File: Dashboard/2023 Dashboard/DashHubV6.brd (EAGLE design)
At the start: 86.4 x 66 mm, 33 parts, among them J1 LEFT, J2 RIGHT, U1 ALLEGRO_MICROSYSTEMS_ACS722LL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, U2 XBEE_PRO_S3B

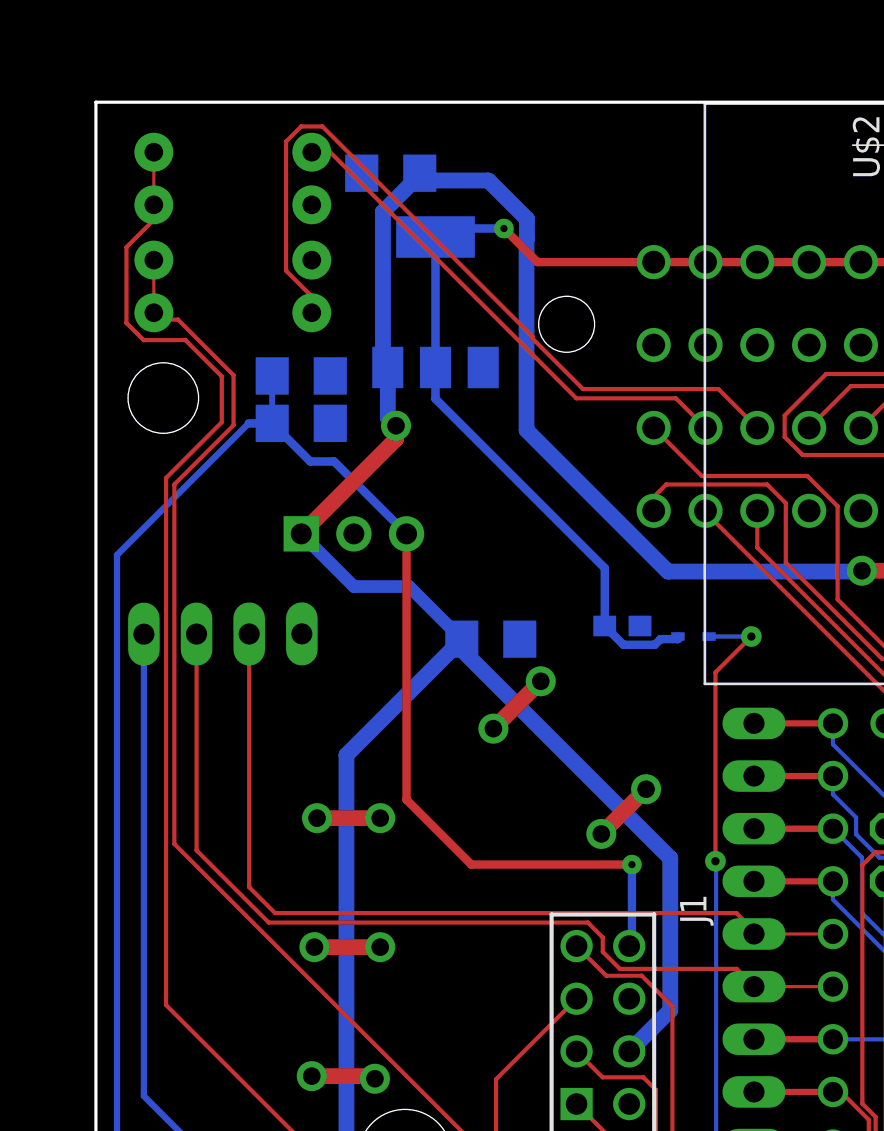
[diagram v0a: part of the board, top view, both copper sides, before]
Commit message: Updated pull ups on dashboard
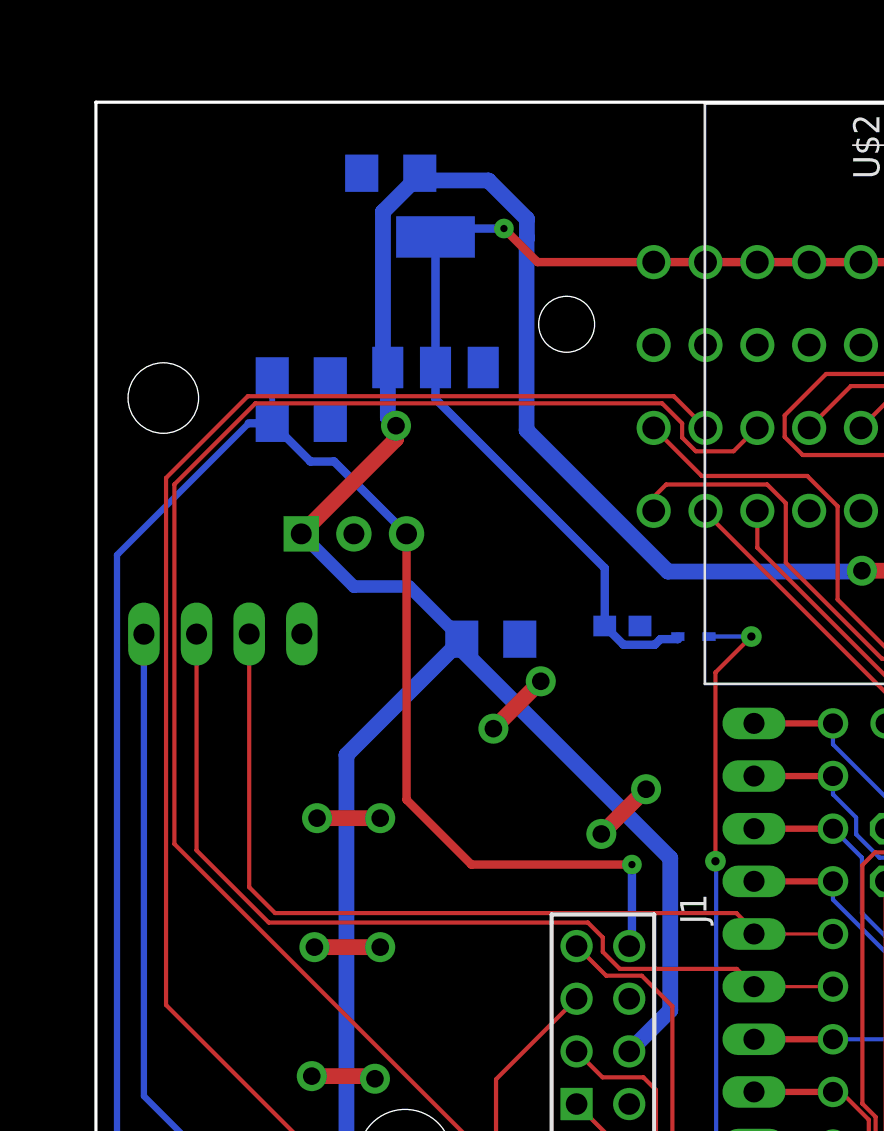
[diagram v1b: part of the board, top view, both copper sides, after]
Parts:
- removed R10, R11: 1.8k, SparkFun-Resistors:AXIAL-0.3
- removed R12, R13: 3.3k, SparkFun-Resistors:AXIAL-0.3
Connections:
- removed net N$23: R10.P$2, U$4.P$3B
- removed net N$24: R11.P$2, U$4.P$3C
- net ENGINE_RPM: now also U$4.P$3B; no longer R10.P$1, R12.P$2
- net GND: no longer R12.P$1, R13.P$1
- net SECONDARY_RPM: now also U$4.P$3C; no longer R11.P$1, R13.P$2
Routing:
- net N$24: track 37.9 -> 0.00 mm
- net N$23: track 24.5 -> 0.00 mm
- net SECONDARY_RPM: track 93.3 -> 110.8 mm
- net ENGINE_RPM: track 104.0 -> 111.8 mm
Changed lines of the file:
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@@
 <attribute name="VALUE" x="8.255" y="-31.242" size="1.27" layer="28" rot="MR90"/>
-</element>
-<element name="R10" library="SparkFun-Resistors" library_urn="urn:adsk.eagle:library:532" package="AXIAL-0.3" package3d_urn="urn:adsk.eagle:package:39658/1" value="1.8k" x="-36.576" y="30.607" smashed="yes" rot="MR180">
-<attribute name="NAME" x="-36.576" y="32.131" size="0.6096" layer="26" font="vector" ratio="20" rot="MR180" align="bottom-center"/>
-<attribute name="PROD_ID" value=" " x="-36.576" y="30.607" size="1.778" layer="28" rot="MR180" display="off"/>
-<attribute name="VALUE" x="-36.576" y="31.623" size="0.6096" layer="28" font="vector" ratio="20" rot="MR180" align="top-center"/>
-</element>
-<element name="R11" library="SparkFun-Resistors" library_urn="urn:adsk.eagle:library:532" package="AXIAL-0.3" package3d_urn="urn:adsk.eagle:package:39658/1" value="1.8k" x="-36.576" y="22.86" smashed="yes" rot="MR180">
-<attribute name="NAME" x="-36.576" y="24.384" size="0.6096" layer="26" font="vector" ratio="20" rot="MR180" align="bottom-center"/>
-<attribute name="PROD_ID" value=" " x="-36.576" y="22.86" size="1.778" layer="28" rot="MR180" display="off"/>
-<attribute name="VALUE" x="-36.576" y="23.876" size="0.6096" layer="28" font="vector" ratio="20" rot="MR180" align="top-center"/>
-</element>
-<element name="R12" library="SparkFun-Resistors" library_urn="urn:adsk.eagle:library:532" package="AXIAL-0.3" package3d_urn="urn:adsk.eagle:package:39658/1" value="3.3k" x="-36.576" y="28.067" smashed="yes" rot="MR0">
-<attribute name="NAME" x="-36.576" y="29.083" size="0.6096" layer="26" font="vector" ratio="20" rot="MR0" align="bottom-center"/>
-<attribute name="PROD_ID" value=" " x="-36.576" y="28.067" size="1.778" layer="28" rot="MR0" display="off"/>
-<attribute name="VALUE" x="-36.576" y="27.051" size="0.6096" layer="28" font="vector" ratio="20" rot="MR0" align="top-center"/>
-</element>
-<element name="R13" library="SparkFun-Resistors" library_urn="urn:adsk.eagle:library:532" package="AXIAL-0.3" package3d_urn="urn:adsk.eagle:package:39658/1" value="3.3k" x="-36.576" y="25.4" smashed="yes" rot="MR0">
-<attribute name="NAME" x="-36.576" y="26.416" size="0.6096" layer="26" font="vector" ratio="20" rot="MR0" align="bottom-center"/>
-<attribute name="PROD_ID" value=" " x="-36.576" y="25.4" size="1.778" layer="28" rot="MR0" display="off"/>
-<attribute name="VALUE" x="-36.576" y="24.384" size="0.6096" layer="28" font="vector" ratio="20" rot="MR0" align="top-center"/>
 </element>
 <element name="JP4" library="pinhead" library_urn="urn:adsk.eagle:library:325" package="2X05" package3d_urn="urn:adsk.eagle:package:22470/2" value="" x="0" y="-3.302" smashed="yes" rot="MR180">
@@
 <contactref element="J1" pad="02"/>
 <contactref element="JP2" pad="14"/>
-<contactref element="R12" pad="P$1"/>
-<contactref element="R13" pad="P$1"/>
 <contactref element="R14" pad="P$1"/>
 <contactref element="R16" pad="P$1"/>
@@
 </signal>
 <signal name="ENGINE_RPM">
-<contactref element="R10" pad="P$1"/>
-<contactref element="R12" pad="P$2"/>
 <contactref element="U$1" pad="22/A8"/>
 <contactref element="JP3" pad="5"/>
-<wire x1="-40.386" y1="30.607" x2="-40.386" y2="28.067" width="0.1524" layer="1"/>
 <wire x1="11.43" y1="-19.812" x2="7.62" y2="-19.812" width="0.3048" layer="1"/>
 <via x="-25.273" y="-21.59" extent="1-16" drill="0.35"/>
 <wire x1="-25.273" y1="-21.59" x2="-28.74636875" y2="-21.59" width="0.2032" layer="1"/>
 <wire x1="-28.74636875" y1="-21.59" x2="-39.796509375" y2="-10.539859375" width="0.2032" layer="1"/>
-<wire x1="-37.1094" y1="19.7860375" x2="-37.1094" y2="17.5773625" width="0.2032" layer="1"/>
-<wire x1="-40.88049375" y1="21.5392" x2="-41.7068" y2="22.36550625" width="0.2032" layer="1"/>
-<wire x1="-40.386" y1="27.34229375" x2="-40.386" y2="28.067" width="0.2032" layer="1"/>
-<wire x1="-41.7068" y1="26.02149375" x2="-40.386" y2="27.34229375" width="0.2032" layer="1"/>
-<wire x1="-37.1094" y1="19.7860375" x2="-38.8625625" y2="21.5392" width="0.2032" layer="1"/>
-<wire x1="-38.8625625" y1="21.5392" x2="-40.88049375" y2="21.5392" width="0.2032" layer="1"/>
-<wire x1="-41.7068" y1="22.36550625" x2="-41.7068" y2="26.02149375" width="0.2032" layer="1"/>
-<wire x1="-37.1094" y1="17.5773625" x2="-39.796509375" y2="14.890253125" width="0.2032" layer="1"/>
-<wire x1="-39.796509375" y1="14.890253125" x2="-39.796509375" y2="-10.539859375" width="0.2032" layer="1"/>
+<wire x1="-39.796509375" y1="-10.539859375" x2="-39.796509375" y2="14.890253125" width="0.2032" layer="1"/>
 <wire x1="-18.1864" y1="-23.4696" x2="3.9624" y2="-23.4696" width="0.2032" layer="16"/>
 <wire x1="3.9624" y1="-23.4696" x2="7.62" y2="-19.812" width="0.2032" layer="16"/>
@@
 <wire x1="-25.018165625" y1="-21.590834375" x2="-25.019" y2="-21.59" width="0.2032" layer="16"/>
 <wire x1="-25.273" y1="-21.59" x2="-25.019" y2="-21.59" width="0.2032" layer="16"/>
+<contactref element="U$4" pad="P$3B"/>
+<wire x1="-39.796509375" y1="14.890253125" x2="-35.85238125" y2="18.83438125" width="0.2032" layer="1"/>
+<wire x1="-35.85238125" y1="18.83438125" x2="-15.30038125" y2="18.83438125" width="0.2032" layer="1"/>
+<wire x1="-15.30038125" y1="18.83438125" x2="-13.77" y2="17.304" width="0.2032" layer="1"/>
 </signal>
 <signal name="AUX_TX">
@@
 </signal>
 <signal name="SECONDARY_RPM">
-<contactref element="R11" pad="P$1"/>
-<contactref element="R13" pad="P$2"/>
 <contactref element="U$1" pad="23/A9"/>
 <contactref element="JP3" pad="4"/>
-<wire x1="-40.386" y1="25.4" x2="-40.386" y2="22.86" width="0.1524" layer="1"/>
 <wire x1="11.43" y1="-22.352" x2="7.62" y2="-22.352" width="0.3048" layer="1"/>
 <via x="-19.177" y="-23.876" extent="1-16" drill="0.35"/>
-<wire x1="-39.2232625" y1="22.5298" x2="-40.0558" y2="22.5298" width="0.2032" layer="1"/>
-<wire x1="-40.0558" y1="22.5298" x2="-40.386" y2="22.86" width="0.2032" layer="1"/>
-<wire x1="-39.2232625" y1="22.5298" x2="-36.54073125" y2="19.84726875" width="0.2032" layer="1"/>
-<wire x1="-36.54073125" y1="19.84726875" x2="-36.54073125" y2="17.43426875" width="0.2032" layer="1"/>
 <wire x1="-39.3942" y1="14.5808" x2="-39.3942" y2="-2.7698" width="0.2032" layer="1"/>
-<wire x1="-36.54073125" y1="17.43426875" x2="-39.3942" y2="14.5808" width="0.2032" layer="1"/>
+<wire x1="-35.4844" y1="18.4906" x2="-39.3942" y2="14.5808" width="0.2032" layer="1"/>
 <wire x1="-39.3942" y1="-2.7698" x2="-24.257" y2="-17.907" width="0.2032" layer="1"/>
 <wire x1="-24.257" y1="-17.907" x2="-24.257" y2="-20.701" width="0.2032" layer="1"/>
@@
 <wire x1="-19.177" y1="-23.876" x2="-19.177" y2="-23.803" width="0.2032" layer="16"/>
 <wire x1="-19.177" y1="-23.803" x2="6.169" y2="-23.803" width="0.2032" layer="16"/>
+<contactref element="U$4" pad="P$3C"/>
+<wire x1="-14.8966" y1="16.83734375" x2="-14.23665625" y2="16.1774" width="0.2032" layer="1"/>
+<wire x1="-14.23665625" y1="16.1774" x2="-12.41434375" y2="16.1774" width="0.2032" layer="1"/>
+<wire x1="-11.28774375" y1="17.304" x2="-11.27" y2="17.304" width="0.2032" layer="1"/>
+<wire x1="-12.41434375" y1="16.1774" x2="-11.28774375" y2="17.304" width="0.2032" layer="1"/>
+<wire x1="-35.4844" y1="18.4906" x2="-15.86334375" y2="18.4906" width="0.2032" layer="1"/>
+<wire x1="-15.86334375" y1="18.4906" x2="-14.8966" y2="17.52385625" width="0.2032" layer="1"/>
+<wire x1="-14.8966" y1="17.52385625" x2="-14.8966" y2="16.83734375" width="0.2032" layer="1"/>
 </signal>
 <signal name="SIN_R">
@@
 <wire x1="11.43" y1="-27.432" x2="7.62" y2="-27.432" width="0.3048" layer="1"/>
 </signal>
-<signal name="N$23">
-<contactref element="R10" pad="P$2"/>
-<contactref element="U$4" pad="P$3B"/>
-<wire x1="-31.877" y1="30.607" x2="-32.766" y2="30.607" width="0.2032" layer="1"/>
-<wire x1="-31.877" y1="30.607" x2="-20.0025" y2="18.7325" width="0.2032" layer="1"/>
-<wire x1="-20.0025" y1="18.7325" x2="-15.1985" y2="18.7325" width="0.2032" layer="1"/>
-<wire x1="-15.1985" y1="18.7325" x2="-13.77" y2="17.304" width="0.2032" layer="1"/>
-</signal>
-<signal name="N$24">
-<contactref element="R11" pad="P$2"/>
-<contactref element="U$4" pad="P$3C"/>
-<wire x1="-34.0074" y1="31.12120625" x2="-33.28020625" y2="31.8484" width="0.2032" layer="1"/>
-<wire x1="-33.28020625" y1="31.8484" x2="-32.25179375" y2="31.8484" width="0.2032" layer="1"/>
-<wire x1="-32.766" y1="22.86" x2="-32.766" y2="23.64439375" width="0.2032" layer="1"/>
-<wire x1="-32.766" y1="23.64439375" x2="-34.0074" y2="24.88579375" width="0.2032" layer="1"/>
-<wire x1="-34.0074" y1="24.88579375" x2="-34.0074" y2="31.12120625" width="0.2032" layer="1"/>
-<wire x1="-22.1216" y1="21.71820625" x2="-22.1216" y2="21.61988125" width="0.2032" layer="1"/>
-<wire x1="-22.1216" y1="21.61988125" x2="-19.67871875" y2="19.177" width="0.2032" layer="1"/>
-<wire x1="-19.67871875" y1="19.177" x2="-13.143" y2="19.177" width="0.2032" layer="1"/>
-<wire x1="-32.25179375" y1="31.8484" x2="-22.1216" y2="21.71820625" width="0.2032" layer="1"/>
-<wire x1="-13.143" y1="19.177" x2="-11.27" y2="17.304" width="0.2032" layer="1"/>
-</signal>
 <signal name="33">

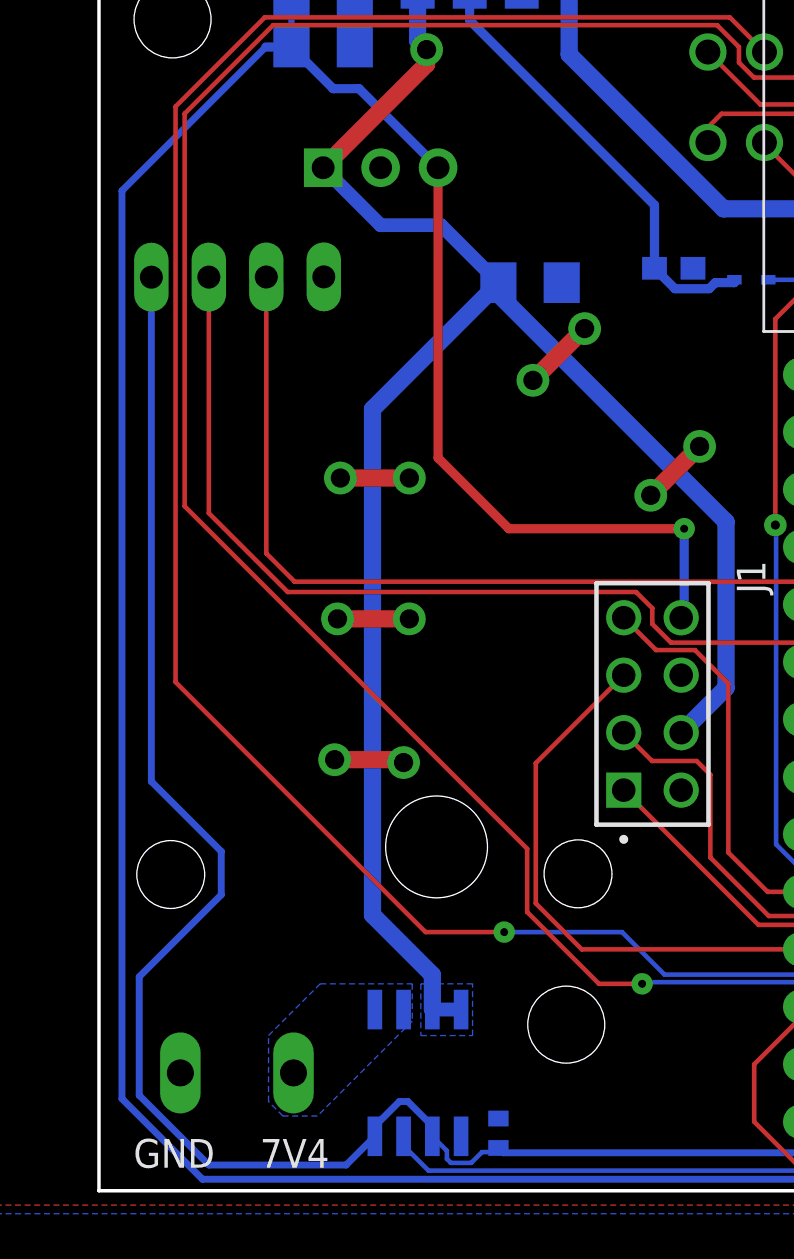
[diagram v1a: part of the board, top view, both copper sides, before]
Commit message: Updated dash hub to power GPS with 5V
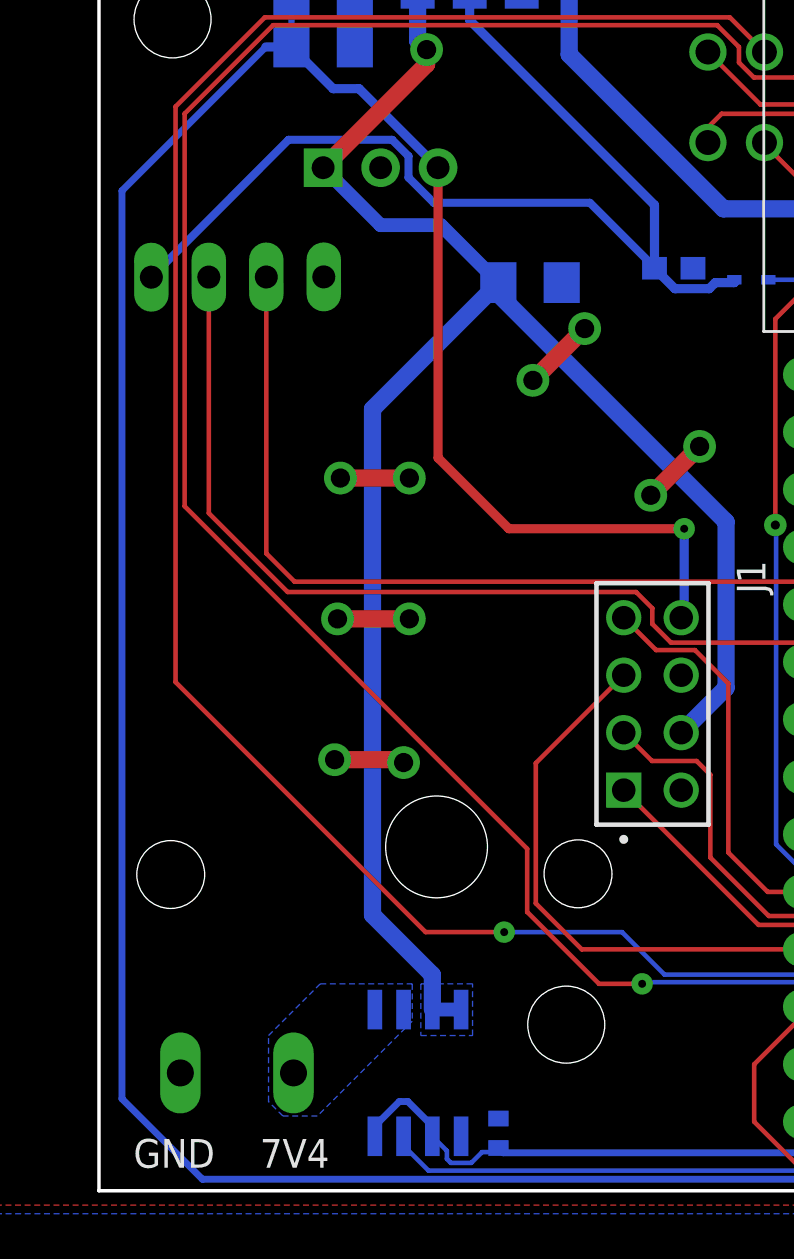
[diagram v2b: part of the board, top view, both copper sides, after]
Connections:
- net 3.3V_TEENSY: no longer U$5.VCC
- net 5V: now also U$5.VCC
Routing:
- net 3.3V_TEENSY: track 210.5 -> 159.3 mm
- net 5V: track 50.2 -> 77.8 mm
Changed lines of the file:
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@@
 <contactref element="U1" pad="6"/>
 <contactref element="U2" pad="1"/>
-<contactref element="U$5" pad="VCC"/>
 <contactref element="U$2" pad="VCC"/>
 <contactref element="U$4" pad="P$1M"/>
@@
 <contactref element="U$4" pad="P$1K"/>
 <contactref element="U$4" pad="P$1J"/>
-<wire x1="-40.865346875" y1="7.35280625" x2="-40.86535" y2="-14.93495625" width="0.3048" layer="16"/>
 <wire x1="-1.27" y1="25.304" x2="1.23" y2="25.304" width="0.4064" layer="1"/>
 <wire x1="1.23" y1="25.304" x2="3.73" y2="25.304" width="0.4064" layer="1"/>
@@
 <wire x1="-30.988" y1="-30.16086875" x2="-30.988" y2="-30.613" width="0.3048" layer="16"/>
 <wire x1="-29.90473125" y1="-29.0776" x2="-30.988" y2="-30.16086875" width="0.3048" layer="16"/>
-<wire x1="-30.988" y1="-30.613" x2="-32.258" y2="-31.883" width="0.3048" layer="16"/>
-<wire x1="-32.258" y1="-31.883" x2="-38.3247" y2="-31.883" width="0.3048" layer="16"/>
-<wire x1="-38.3247" y1="-31.883" x2="-41.402" y2="-28.8057" width="0.3048" layer="16"/>
-<wire x1="-41.402" y1="-28.8057" x2="-41.402" y2="-23.56615625" width="0.3048" layer="16"/>
-<wire x1="-37.77586875" y1="-19.940025" x2="-37.77586875" y2="-18.0244375" width="0.3048" layer="16"/>
-<wire x1="-41.402" y1="-23.56615625" x2="-37.77586875" y2="-19.940025" width="0.3048" layer="16"/>
-<wire x1="-37.77586875" y1="-18.0244375" x2="-40.86535" y2="-14.93495625" width="0.3048" layer="16"/>
 <wire x1="24.638" y1="-22.186" x2="37.25" y2="-22.186" width="0.3048" layer="1"/>
 <wire x1="37.25" y1="-22.186" x2="39.116" y2="-20.32" width="0.3048" layer="1"/>
@@
 <wire x1="-18.63" y1="7.747" x2="-17.7268" y2="6.8438" width="0.4064" layer="16"/>
 <wire x1="-17.7268" y1="6.8438" x2="-16.2129875" y2="6.8438" width="0.4064" layer="16"/>
+<contactref element="U$5" pad="VCC"/>
+<wire x1="-29.5012" y1="12.70264375" x2="-30.22335625" y2="13.4248" width="0.3556" layer="16"/>
+<wire x1="-34.8012375" y1="13.424346875" x2="-40.865346875" y2="7.35280625" width="0.3556" layer="16"/>
+<wire x1="-28.38804375" y1="10.6426" x2="-29.5012" y2="11.75575625" width="0.3556" layer="16"/>
+<wire x1="-29.5012" y1="11.75575625" x2="-29.5012" y2="12.70264375" width="0.3556" layer="16"/>
+<wire x1="-18.63" y1="7.747" x2="-18.63" y2="7.7862875" width="0.3556" layer="16"/>
+<wire x1="-18.63" y1="7.7862875" x2="-21.4863125" y2="10.6426" width="0.3556" layer="16"/>
+<wire x1="-21.4863125" y1="10.6426" x2="-28.38804375" y2="10.6426" width="0.3556" layer="16"/>
+<wire x1="-30.22335625" y1="13.4248" x2="-34.8012375" y2="13.424346875" width="0.3556" layer="16"/>
 </signal>
 <signal name="3.3V_REG">

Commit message: Update dashboard pcb files
Removed xbee and current sensor
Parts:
- removed C1: 0.1uF, rcl:C0402
- removed U1: ALLEGRO_MICROSYSTEMS_ACS722LLCTR-05AB-TALLEGRO_MICROSYSTEMS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, Allegro MicroSystems - ACS722LLCTR-05AB-T:ALLEGRO_MICROSYSTEMS_ACS722LLCTR-05AB-T_0
- removed U2: XBEE_PRO_S3B, GTOR - Microcontroller:XBEE_PRO_S3B
- moved R1 2.87 mm to (19.3, -20.7)
- moved R2 2.87 mm to (21.8, -20.7)
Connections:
- removed net LIPO_IN: LIPO.1, U1.1, U1.2
- net 3.3V_TEENSY: no longer C1.2, U1.6, U1.8, U2.1
- net 7.4V: now also LIPO.1; no longer U1.3, U1.4
- net CURR_SENSE: no longer U1.7
- net GND: no longer C1.1, U1.5, U2.10
- net XBEE_RX: no longer U2.3
- net XBEE_TX: no longer U2.2
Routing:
- net XBEE_RX: track 107.6 -> 3.81 mm
- net XBEE_TX: track 92.3 -> 3.81 mm
- net CURR_SENSE: track 88.4 -> 3.81 mm
- net 3.3V_TEENSY: track 159.3 -> 90.8 mm
- net 31: track 41.3 -> 28.9 mm
- net 3.3V_REG: track 177.4 -> 170.6 mm
- net N$2: track 68.6 -> 61.8 mm, vias 2 -> 0
- net SCL_OLED: track 138.4 -> 132.0 mm
- net SDA_OLED: track 122.1 -> 116.3 mm
- net ANALOG1: track 81.0 -> 78.2 mm
- net ANALOG3: track 130.2 -> 127.4 mm
- net GPS_RX: track 41.4 -> 39.0 mm
- net GPS_TX: track 44.3 -> 42.0 mm
- net AUX_RX: track 56.5 -> 54.3 mm
- net ANALOG2: track 76.2 -> 74.3 mm
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- removed copper zone on layer 16, net 7.4V
